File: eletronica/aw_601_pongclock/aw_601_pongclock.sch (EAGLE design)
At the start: 66 parts, among them IC1 MEGA8-P, IC2 4515N, IC3 4515N, IC4 4094N, IC5 4094N, IC6 4094N, IC7 4094N, J9 DCJ0202, Q1 8Mhz?

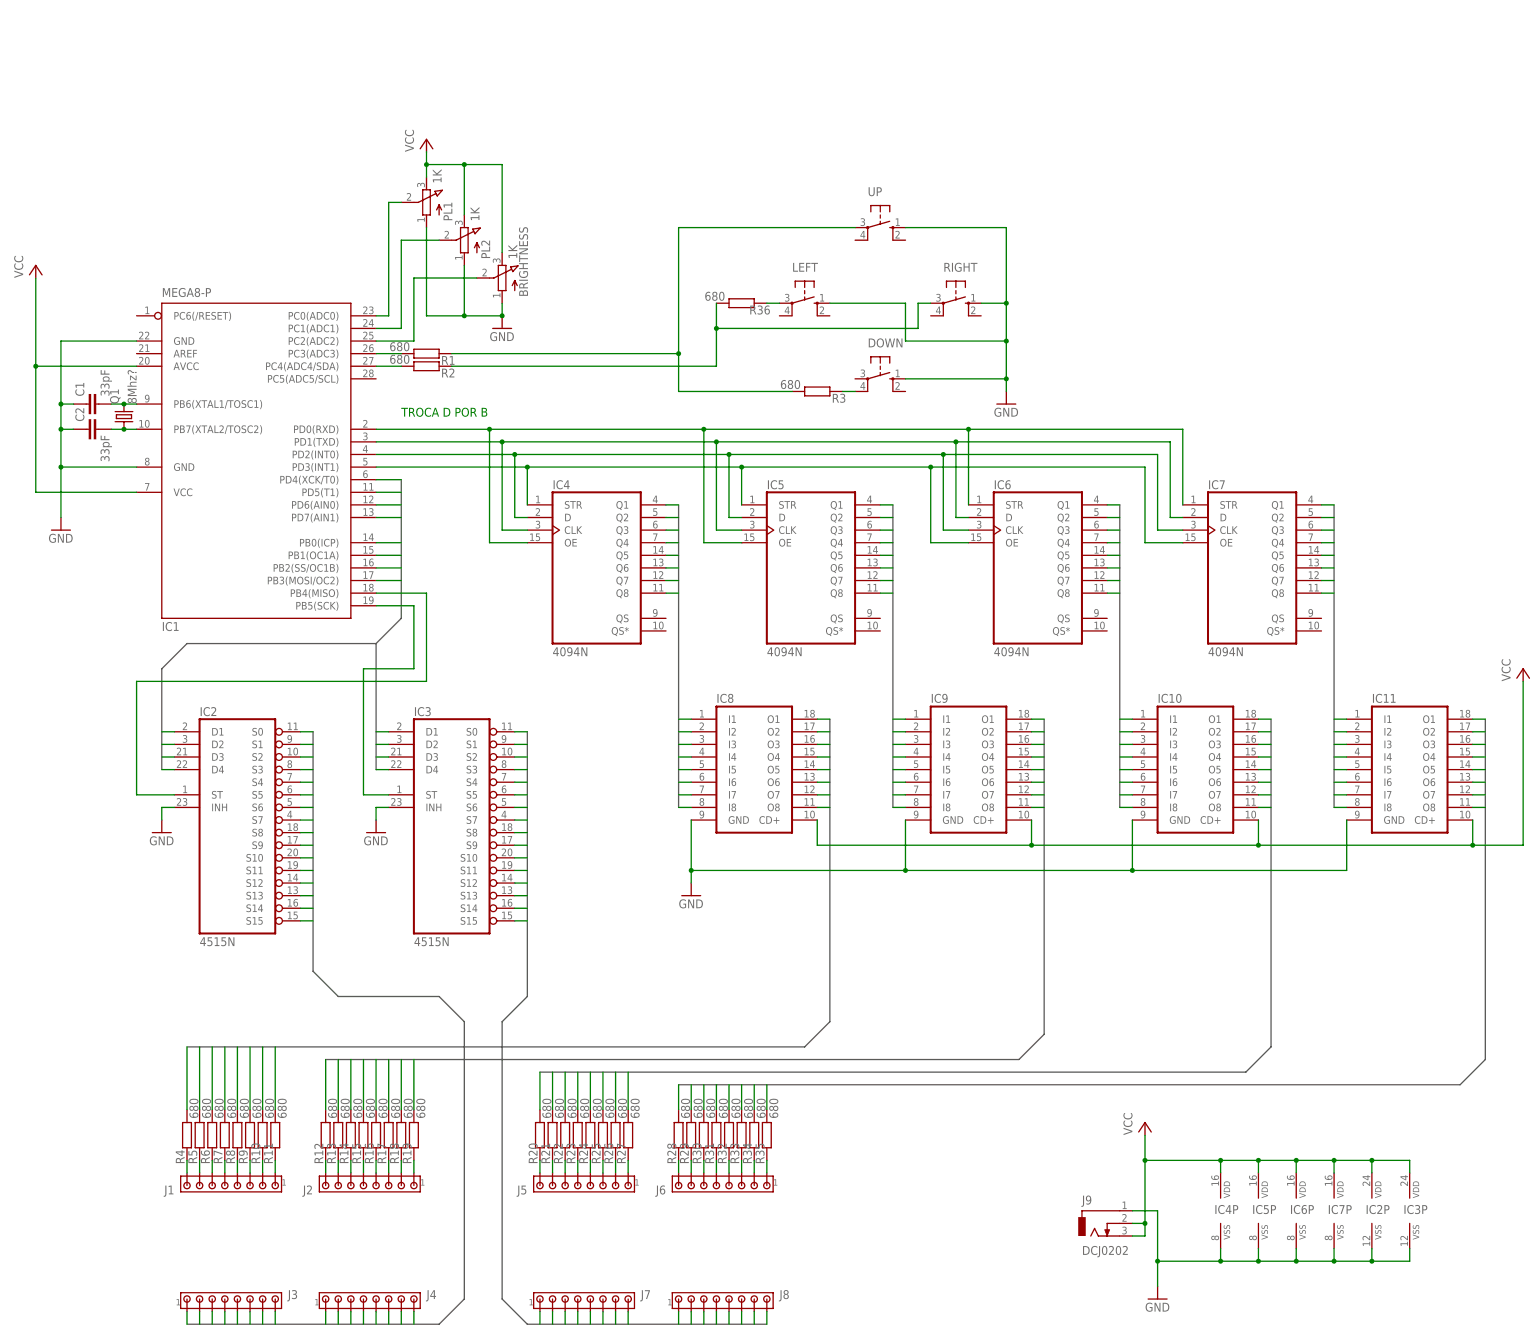
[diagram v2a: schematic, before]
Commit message: 
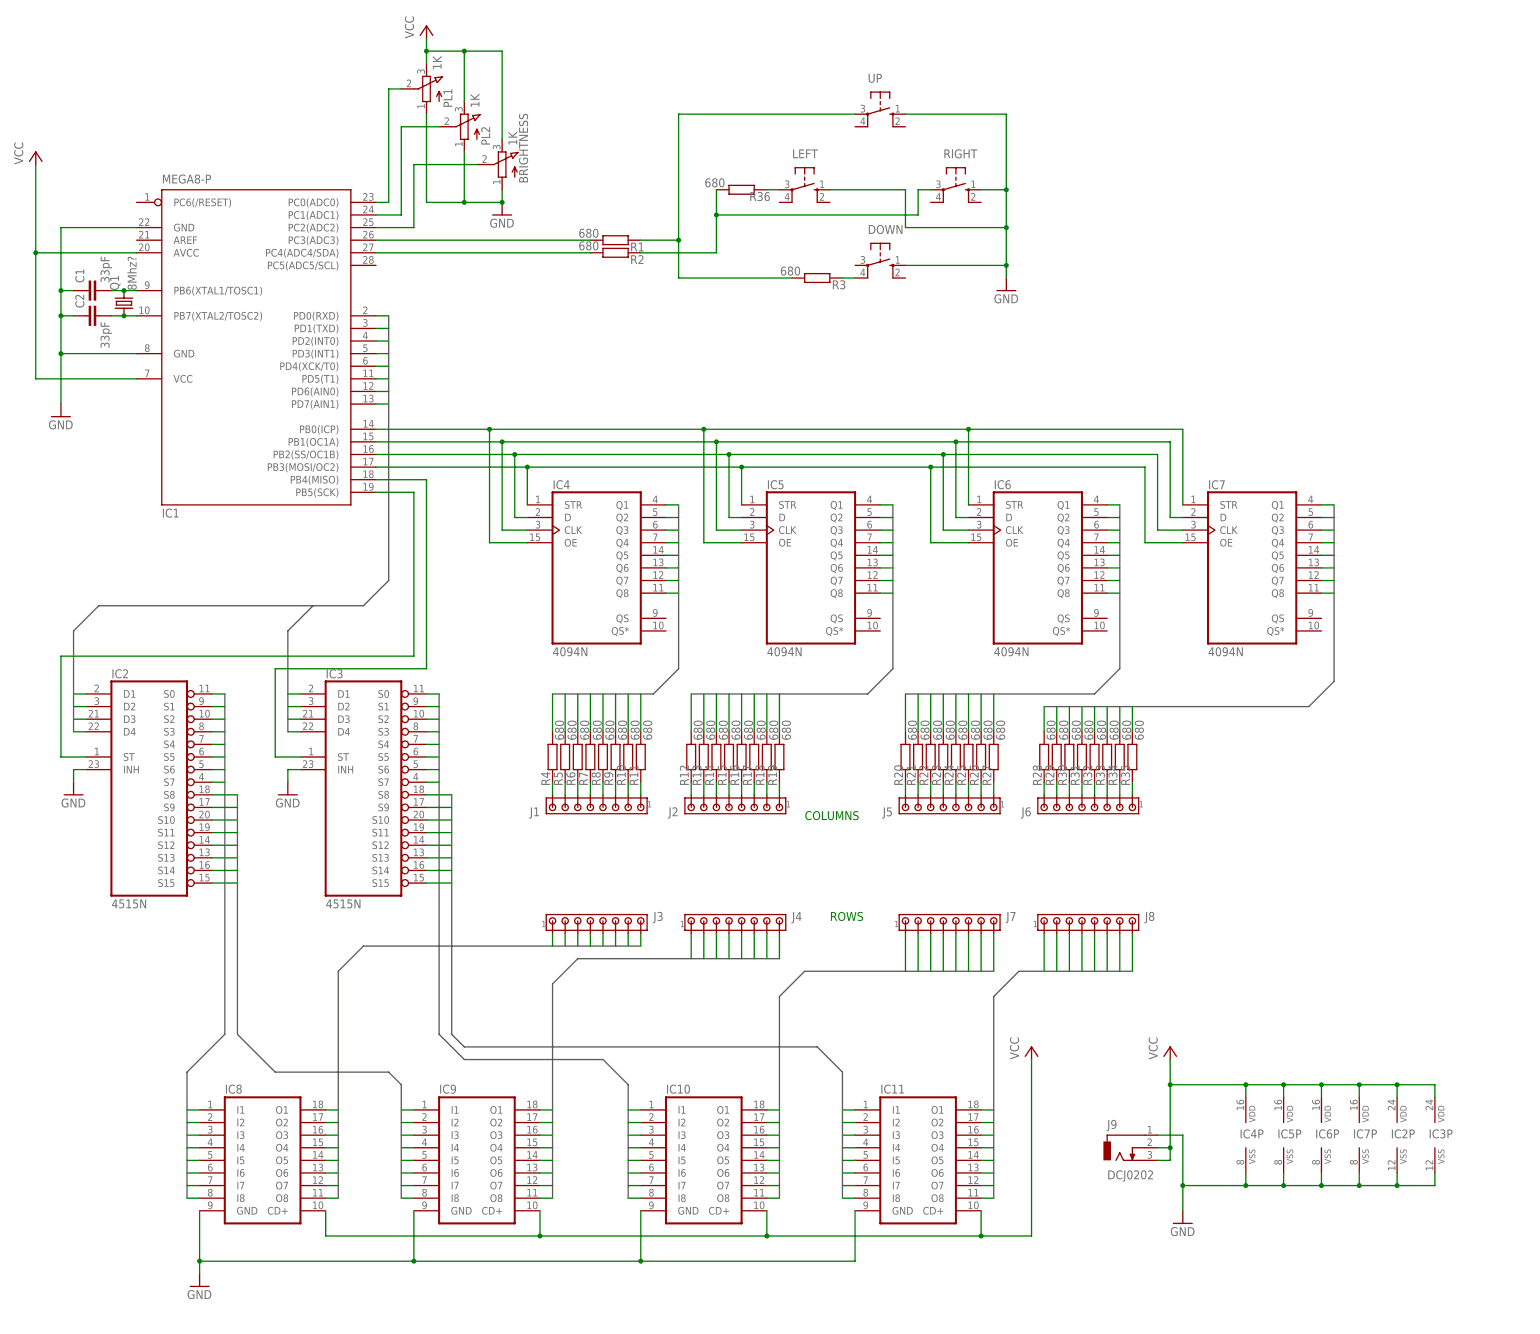
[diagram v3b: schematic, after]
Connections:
- removed net CATH1_10: IC2A.S10, J4.3
- removed net CATH1_11: IC2A.S11, J4.4
- removed net CATH1_12: IC2A.S12, J4.5
- removed net CATH1_13: IC2A.S13, J4.6
- removed net CATH1_14: IC2A.S14, J4.7
- removed net CATH1_15: IC2A.S15, J4.8
- removed net CATH1_8: IC2A.S8, J4.1
- removed net CATH1_9: IC2A.S9, J4.2
- removed net CATH2_10: IC3A.S10, J8.3
- removed net CATH2_11: IC3A.S11, J8.4
- removed net CATH2_12: IC3A.S12, J8.5
- removed net CATH2_13: IC3A.S13, J8.6
- removed net CATH2_14: IC3A.S14, J8.7
- removed net CATH2_15: IC3A.S15, J8.8
- removed net CATH2_8: IC3A.S8, J8.1
- removed net CATH2_9: IC3A.S9, J8.2
- new net CATH1B_0: IC9.O1, J4.1
- new net CATH1B_1: IC9.O2, J4.2
- new net CATH1B_2: IC9.O3, J4.3
- new net CATH1B_3: IC9.O4, J4.4
- new net CATH1B_4: IC9.O5, J4.5
- new net CATH1B_5: IC9.O6, J4.6
- new net CATH1B_6: IC9.O7, J4.7
- new net CATH1B_7: IC9.O8, J4.8
- new net CATH2B_0: IC11.O1, J8.1
- new net CATH2B_1: IC11.O2, J8.2
- new net CATH2B_2: IC11.O3, J8.3
- new net CATH2B_3: IC11.O4, J8.4
- new net CATH2B_4: IC11.O5, J8.5
- new net CATH2B_5: IC11.O6, J8.6
- new net CATH2B_6: IC11.O7, J8.7
- new net CATH2B_7: IC11.O8, J8.8
- net CATH1_0: now also IC8.O1; no longer IC2A.S0
- net CATH1_1: now also IC8.O2; no longer IC2A.S1
- net CATH1_2: now also IC8.O3; no longer IC2A.S2
- net CATH1_3: now also IC8.O4; no longer IC2A.S3
- net CATH1_4: now also IC8.O5; no longer IC2A.S4
- net CATH1_5: now also IC8.O6; no longer IC2A.S5
- net CATH1_6: now also IC8.O7; no longer IC2A.S6
- net CATH1_7: now also IC8.O8; no longer IC2A.S7
- net CATH2_0: now also IC10.O1; no longer IC3A.S0
- net CATH2_1: now also IC10.O2; no longer IC3A.S1
- net CATH2_2: now also IC10.O3; no longer IC3A.S2
- net CATH2_3: now also IC10.O4; no longer IC3A.S3
- net CATH2_4: now also IC10.O5; no longer IC3A.S4
- net CATH2_5: now also IC10.O6; no longer IC3A.S5
- net CATH2_6: now also IC10.O7; no longer IC3A.S6
- net CATH2_7: now also IC10.O8; no longer IC3A.S7
- net LED1A1: now also IC2A.S0; no longer IC4A.Q1
- net LED1A2: now also IC2A.S1; no longer IC4A.Q2
- net LED1A3: now also IC2A.S2; no longer IC4A.Q3
- net LED1A4: now also IC2A.S3; no longer IC4A.Q4
- net LED1A5: now also IC2A.S4; no longer IC4A.Q5
- net LED1A6: now also IC2A.S5; no longer IC4A.Q6
- net LED1A7: now also IC2A.S6; no longer IC4A.Q7
- net LED1A8: now also IC2A.S7; no longer IC4A.Q8
- net LED1B1: now also IC2A.S8; no longer IC5A.Q1
- net LED1B2: now also IC2A.S9; no longer IC5A.Q2
- net LED1B3: now also IC2A.S10; no longer IC5A.Q3
- net LED1B4: now also IC2A.S11; no longer IC5A.Q4
- net LED1B5: now also IC2A.S12; no longer IC5A.Q5
- net LED1B6: now also IC2A.S13; no longer IC5A.Q6
- net LED1B7: now also IC2A.S14; no longer IC5A.Q7
- net LED1B8: now also IC2A.S15; no longer IC5A.Q8
- net LED2A1: now also IC3A.S0; no longer IC6A.Q1
- net LED2A2: now also IC3A.S1; no longer IC6A.Q2
- net LED2A3: now also IC3A.S2; no longer IC6A.Q3
- net LED2A4: now also IC3A.S3; no longer IC6A.Q4
- net LED2A5: now also IC3A.S4; no longer IC6A.Q5
- net LED2A6: now also IC3A.S5; no longer IC6A.Q6
- net LED2A7: now also IC3A.S6; no longer IC6A.Q7
- net LED2A8: now also IC3A.S7; no longer IC6A.Q8
- net LED2B1: now also IC3A.S8; no longer IC7A.Q1
- net LED2B2: now also IC3A.S9; no longer IC7A.Q2
- net LED2B3: now also IC3A.S10; no longer IC7A.Q3
- net LED2B4: now also IC3A.S11; no longer IC7A.Q4
- net LED2B5: now also IC3A.S12; no longer IC7A.Q5
- net LED2B6: now also IC3A.S13; no longer IC7A.Q6
- net LED2B7: now also IC3A.S14; no longer IC7A.Q7
- net LED2B8: now also IC3A.S15; no longer IC7A.Q8
- net LEDGND0: now also IC1.PD0(RXD); no longer IC1.PD4(XCK/T0)
- net LEDGND1: now also IC1.PD1(TXD); no longer IC1.PD5(T1)
- net LEDGND2: now also IC1.PD2(INT0); no longer IC1.PD6(AIN0)
- net LEDGND3: now also IC1.PD3(INT1); no longer IC1.PD7(AIN1)
- net LEDGND4: now also IC1.PD4(XCK/T0); no longer IC1.PB0(ICP)
- net LEDGND5: now also IC1.PD5(T1); no longer IC1.PB1(OC1A)
- net LEDGND6: now also IC1.PD6(AIN0); no longer IC1.PB2(SS/OC1B)
- net LEDGND7: now also IC1.PD7(AIN1); no longer IC1.PB3(MOSI/OC2)
- net N$1: now also IC1.PB0(ICP); no longer IC1.PD0(RXD)
- net N$2: now also IC1.PB1(OC1A); no longer IC1.PD1(TXD)
- net N$3: now also IC1.PB2(SS/OC1B); no longer IC1.PD2(INT0)
- net N$37: now also IC3A.ST; no longer IC2A.ST
- net N$38: now also IC2A.ST; no longer IC3A.ST
- net N$4: now also IC1.PB3(MOSI/OC2); no longer IC1.PD3(INT1)
- net TRAN1A1: now also IC4A.Q1; no longer IC8.O1
- net TRAN1A2: now also IC4A.Q2; no longer IC8.O2
- net TRAN1A3: now also IC4A.Q3; no longer IC8.O3
- net TRAN1A4: now also IC4A.Q4; no longer IC8.O4
- net TRAN1A5: now also IC4A.Q5; no longer IC8.O5
- net TRAN1A6: now also IC4A.Q6; no longer IC8.O6
- net TRAN1A7: now also IC4A.Q7; no longer IC8.O7
- net TRAN1A8: now also IC4A.Q8; no longer IC8.O8
- net TRAN1B1: now also IC6A.Q1; no longer IC10.O1
- net TRAN1B2: now also IC6A.Q2; no longer IC10.O2
- net TRAN1B3: now also IC6A.Q3; no longer IC10.O3
- net TRAN1B4: now also IC6A.Q4; no longer IC10.O4
- net TRAN1B5: now also IC6A.Q5; no longer IC10.O5
- net TRAN1B6: now also IC6A.Q6; no longer IC10.O6
- net TRAN1B7: now also IC6A.Q7; no longer IC10.O7
- net TRAN1B8: now also IC6A.Q8; no longer IC10.O8
- net TRAN2A1: now also IC5A.Q1; no longer IC9.O1
- net TRAN2A2: now also IC5A.Q2; no longer IC9.O2
- net TRAN2A3: now also IC5A.Q3; no longer IC9.O3
- net TRAN2A4: now also IC5A.Q4; no longer IC9.O4
- net TRAN2A5: now also IC5A.Q5; no longer IC9.O5
- net TRAN2A6: now also IC5A.Q6; no longer IC9.O6
- net TRAN2A7: now also IC5A.Q7; no longer IC9.O7
- net TRAN2A8: now also IC5A.Q8; no longer IC9.O8
- net TRAN2B1: now also IC7A.Q1; no longer IC11.O1
- net TRAN2B2: now also IC7A.Q2; no longer IC11.O2
- net TRAN2B3: now also IC7A.Q3; no longer IC11.O3
- net TRAN2B4: now also IC7A.Q4; no longer IC11.O4
- net TRAN2B5: now also IC7A.Q5; no longer IC11.O5
- net TRAN2B6: now also IC7A.Q6; no longer IC11.O6
- net TRAN2B7: now also IC7A.Q7; no longer IC11.O7
- net TRAN2B8: now also IC7A.Q8; no longer IC11.O8
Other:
- note added: "COLUMNS"
- note added: "ROWS"
- note removed: "TROCA D POR B"
- moved on the sheet: BRIGHTNESS, C1, C2, DOWN, IC1, IC10, IC11, IC2, IC2P, IC3, IC3P, IC4P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

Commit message: 
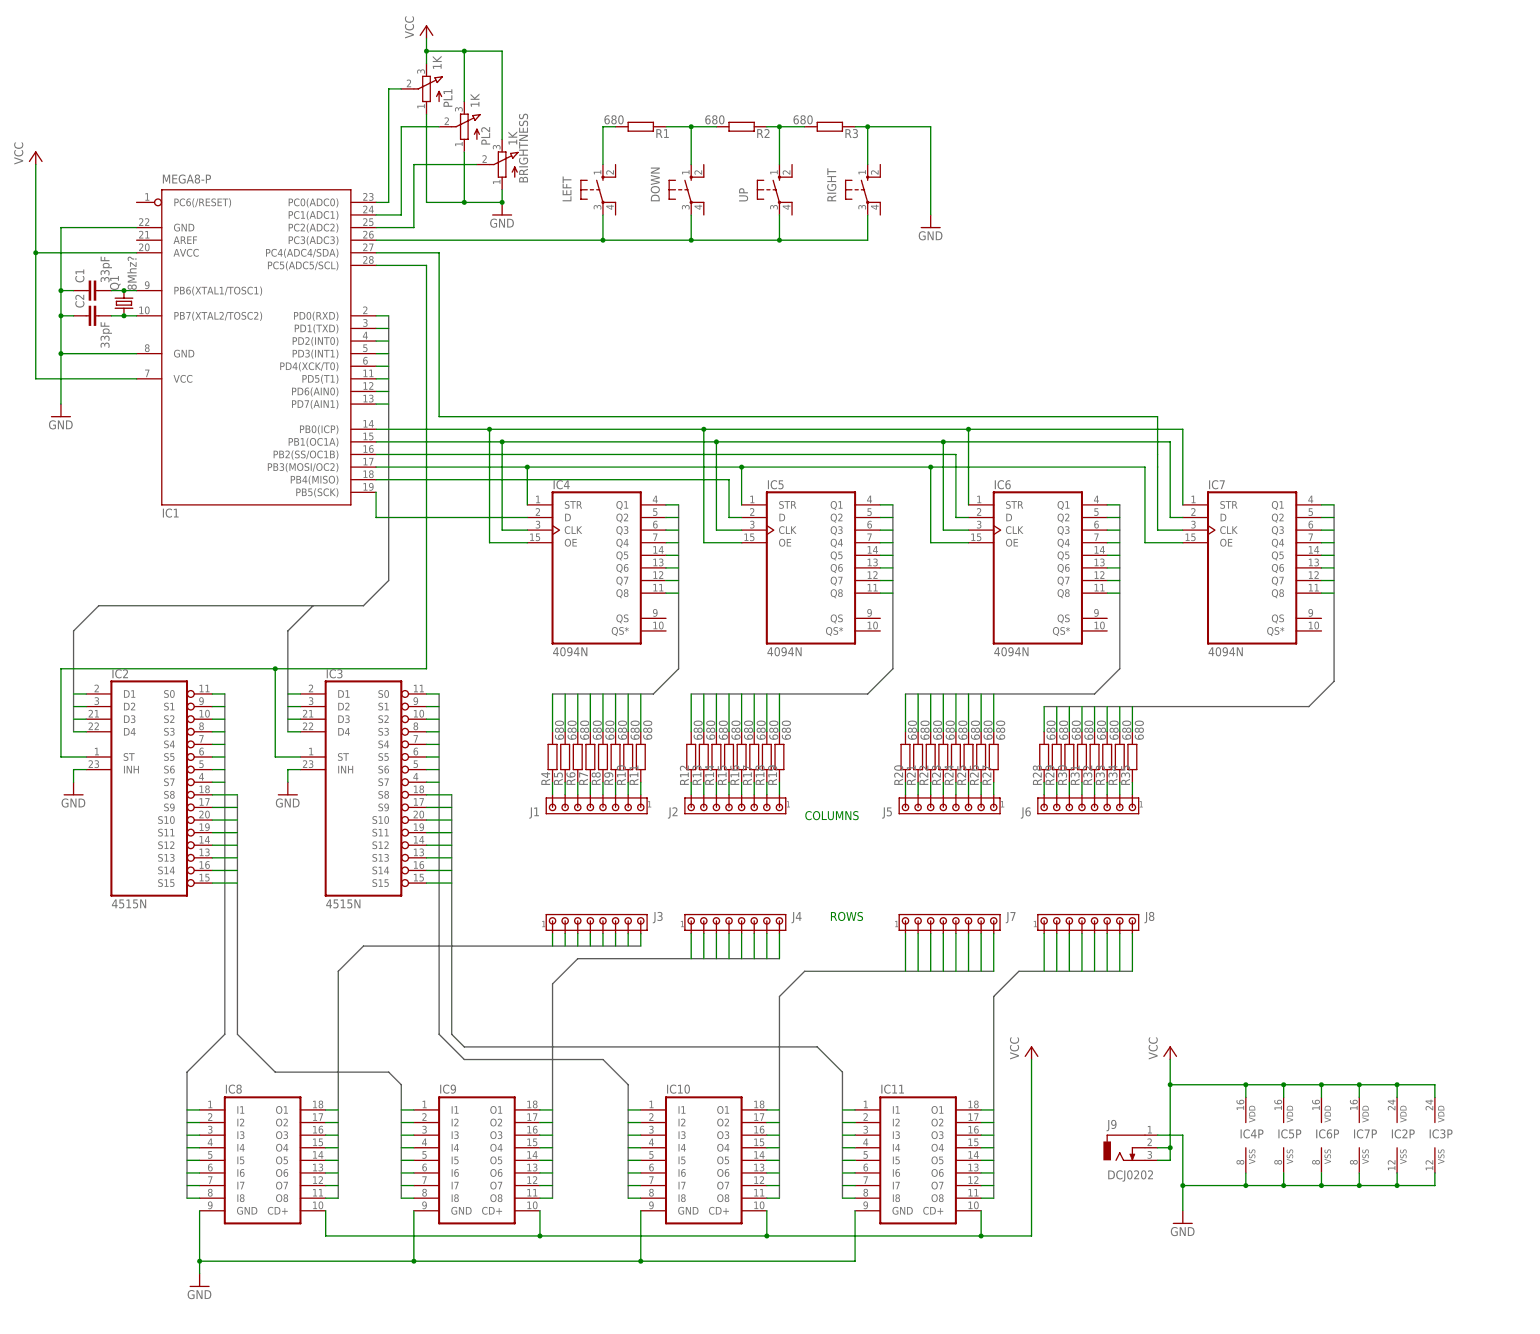
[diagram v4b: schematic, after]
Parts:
- removed R36: 680, rcl:R-EU_0207/10
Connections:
- removed net N$47: R1.1, R3.2, UP.P
- removed net N$49: LEFT.P, R36.1
- removed net N$50: R2.1, R36.2, RIGHT.P
- new net N$46: IC1.PC5(ADC5/SCL), IC2A.ST, IC3A.ST
- new net N$51: IC1.PB2(SS/OC1B), IC6A.D
- new net N$52: IC1.PB1(OC1A), IC4A.CLK, IC5A.CLK, IC6A.CLK, IC7A.D
- net GND: now also R3.1; no longer DOWN.S, LEFT.S, UP.S
- net N$2: now also LEFT.S, R1.2; no longer IC1.PB1(OC1A), IC4A.CLK, IC5A.CLK, IC6A.D, IC7A.D
- net N$3: now also IC1.PC4(ADC4/SDA); no longer IC1.PB2(SS/OC1B), IC4A.D, IC5A.D, IC6A.CLK
- net N$37: now also IC5A.D; no longer IC3A.ST
- net N$38: now also IC4A.D; no longer IC2A.ST
- net N$44: now also DOWN.S, R1.1, R2.2; no longer IC1.PC3(ADC3), R1.2
- net N$45: now also R2.1, R3.2, UP.S; no longer IC1.PC4(ADC4/SDA), R2.2
- net N$48: now also DOWN.P, IC1.PC3(ADC3), LEFT.P, RIGHT.P, UP.P; no longer DOWN.P1, R3.1
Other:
- moved on the sheet: DOWN, LEFT, R1, R2, R3, RIGHT, UP
